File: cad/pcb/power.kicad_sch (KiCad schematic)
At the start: 12 parts

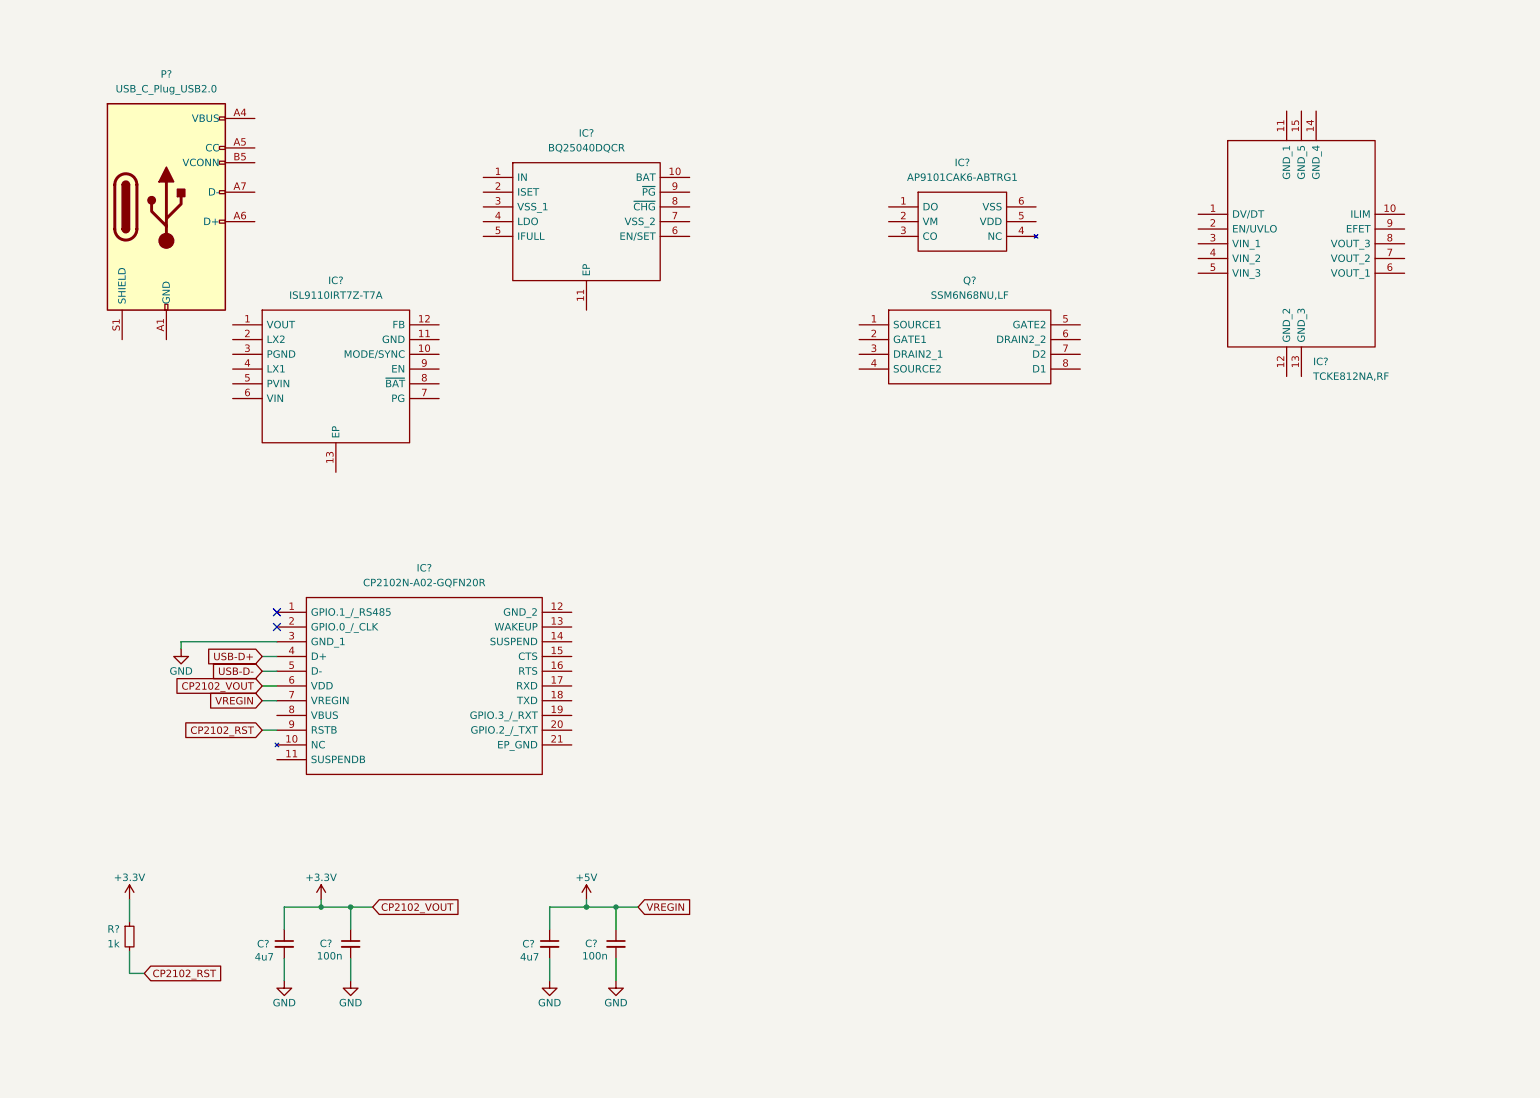
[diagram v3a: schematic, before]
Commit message: add charging & preotection circuit
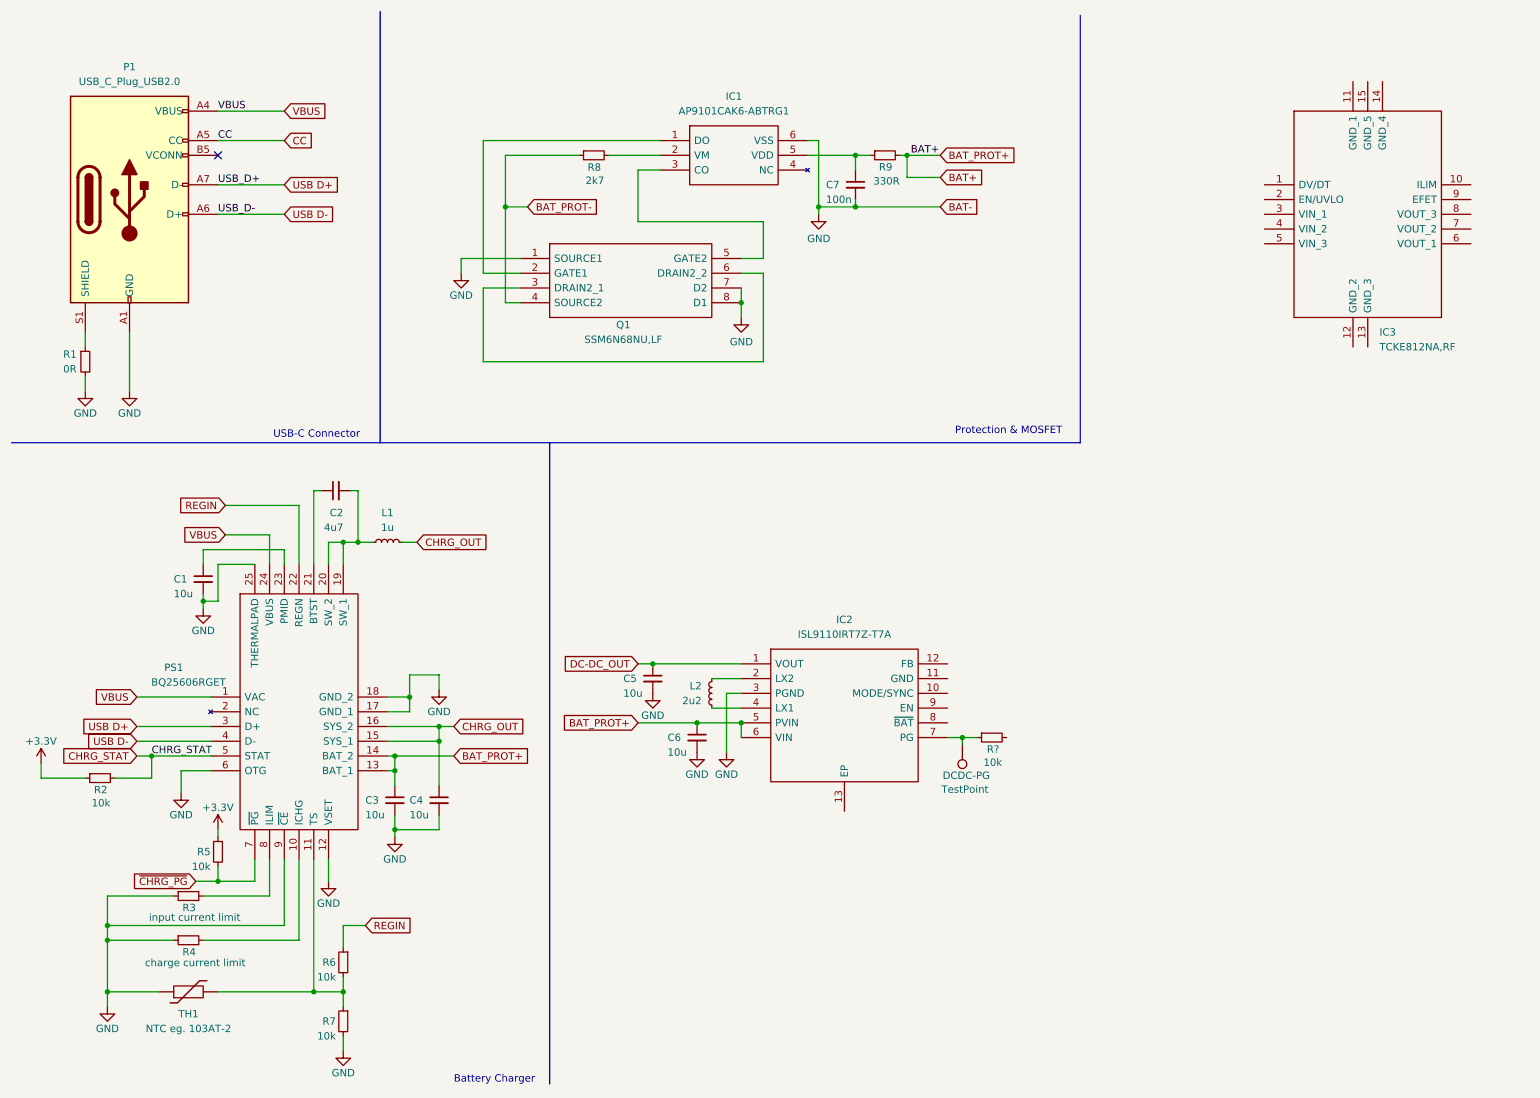
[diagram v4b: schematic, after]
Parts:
- removed C? (x2): 4u7, symbol Device:C_Small
- removed C? (x2): 100n, symbol Device:C_Small
- removed IC?: BQ25040DQCR, SON50P200X300X80-11N, symbol Battery Charger:BQ25040DQCR
- removed IC?: CP2102N-A02-GQFN20R, CP2102NA02GQFN20, symbol USB-UART Bridge:CP2102N-A02-GQFN20R
- removed R?: 1k, symbol Device:R_Small
- added C1, C3, C4, C5, C6: 10u, symbol Device:C_Small
- added C2: 4u7, symbol Device:C_Small
- added C7: 100n, symbol Device:C_Small
- added DCDC-PG: TestPoint, TestPoint:TestPoint_Pad_D2.5mm, symbol Connector:TestPoint
- added L1: 1u, symbol Device:L_Small
- added L2: 2u2, symbol Device:L_Small
- added PS1: BQ25606RGET, QFN50P400X400X100-25N, symbol Battery Charger:BQ25606RGET
- added R1: 0R, symbol Device:R_Small
- added R2, R5, R6, R7, R?: 10k, symbol Device:R_Small
- added R3: input current limit, symbol Device:R_Small
- added R4: charge current limit, symbol Device:R_Small
- added R8: 2k7, symbol Device:R_Small
- added R9: 330R, symbol Device:R_Small
- added TH1: NTC eg. 103AT-2, symbol Device:Thermistor
- gave numbers to parts that had none: 5
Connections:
- net +3.3V: now also R2.1, R5.1
- net GND: now also IC1.6 (VSS), IC2.3 (PGND), P1.A1 (GND), P1.A12 (GND), P1.B1 (GND), P1.B12 (GND), Q1.1 (SOURCE1), Q1.7 (D2), Q1.8 (D1), C1.2, C3.2, C4.2, C5.2, C6.2, C7.2, PS1.12 (VSET), PS1.17 (GND_1), PS1.18 (GND_2), PS1.25 (THERMALPAD), PS1.6 (OTG), PS1.9 (~{CE}), R1.2, R3.1, R4.1, R7.2, TH1.1
- net DC-DC_OUT: now reaches IC2.1 (VOUT)
- net DC-DC_OUT: now also C5.1
- net at IC2.2 (LX2): now also L2.1
- net at IC2.4 (LX1): now also L2.2
- net BAT+: now reaches IC2.5 (PVIN)
- net BAT+: now also IC2.6 (VIN), C3.1, C6.1, PS1.13 (BAT_1), PS1.14 (BAT_2), R9.2
- net at IC2.7 (PG): now also DCDC-PG.1, R?.1
- net VBUS: now reaches P1.A4 (VBUS), P1.A9 (VBUS), P1.B4 (VBUS), P1.B9 (VBUS)
- net VBUS: now also PS1.1 (VAC), PS1.24 (VBUS)
- net CC: now reaches P1.A5 (CC)
- net USB D-: now reaches P1.A6 (D+)
- net USB D-: now also PS1.4 (D-)
- net USB D+: now reaches P1.A7 (D-)
- net USB D+: now also PS1.3 (D+)
- net at P1.S1 (SHIELD): now also R1.1
- net at Q1.2 (GATE1): now also IC1.1 (DO)
- net at Q1.3 (DRAIN2_1): now also Q1.6 (DRAIN2_2)
- net BAT_PROT-: now reaches Q1.4 (SOURCE2)
- net BAT_PROT-: now also R8.1
- net at Q1.5 (GATE2): now also IC1.3 (CO)
- net at IC1.2 (VM): now also R8.2
- net at IC1.5 (VDD): now also C7.1, R9.1
- new net: PS1.11 (TS), R6.2, R7.1, TH1.2
- new net: C1.1, PS1.23 (PMID)
- new net: C2.1, PS1.21 (BTST)
- new net: C2.2, L1.1, PS1.19 (SW_1), PS1.20 (SW_2)
- new net: PS1.10 (ICHG), R4.2
- new net: PS1.8 (ILIM), R3.2
- new net CHRG_OUT: C4.1, L1.2, PS1.15 (SYS_1), PS1.16 (SYS_2)
- new net CHRG_STAT: PS1.5 (STAT), R2.2
- new net REGIN: PS1.22 (REGN), R6.1
- new net ~{CHRG_PG}: PS1.7 (~{PG}), R5.2
- no-connect marks 2 -> 1
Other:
- note added: "Battery Charger"
- note added: "Protection & MOSFET"
- note added: "USB-C Connector"
- moved on the sheet: IC1, IC2, IC3, P1, Q1

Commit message: add dc-dc converter, add sensors
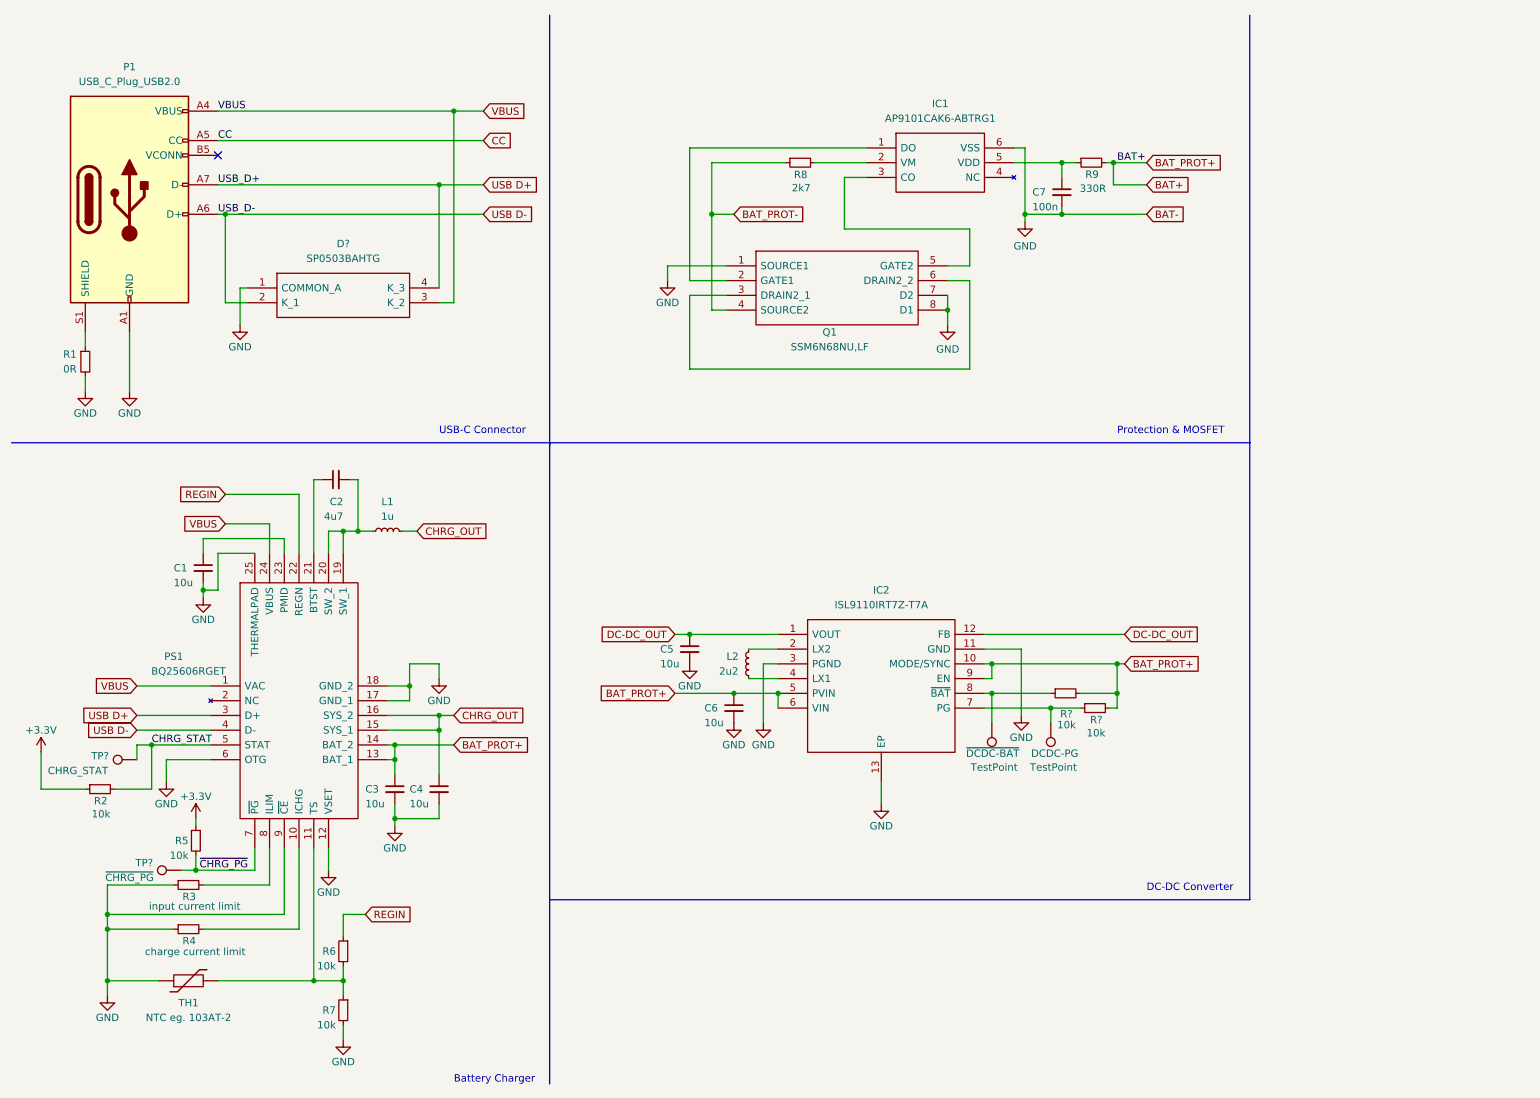
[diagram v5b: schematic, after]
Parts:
- removed IC3: TCKE812NA,RF, TCKE812NARF, symbol eFuse:TCKE812NA,RF
- added D?: SP0503BAHTG, SP0503BAHTG, symbol ESD Protection:SP0503BAHTG
- added R?: 10k, symbol Device:R_Small
- added TP?: CHRG_STAT, symbol Connector:TestPoint
- added TP?: ~{CHRG_PG}, symbol Connector:TestPoint
- added ~{DCDC-BAT}: TestPoint, TestPoint:TestPoint_Pad_D2.5mm, symbol Connector:TestPoint
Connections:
- net BAT+: now also IC2.10 (MODE/SYNC), IC2.9 (EN), R?.2, R?.2
- net CHRG_STAT: now also TP?.1
- net DC-DC_OUT: now also IC2.12 (FB)
- net GND: now also IC2.11 (GND), IC2.13 (EP), D?.1 (COMMON_A)
- net USB D+: now also D?.4 (K_3)
- net USB D-: now also D?.2 (K_1)
- net VBUS: now also D?.3 (K_2)
- net ~{CHRG_PG}: now also TP?.1
- net at IC2.8 (~{BAT}): now also R?.1, ~{DCDC-BAT}.1
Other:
- note added: "DC-DC Converter"
- moved on the sheet: C1, C2, C3, C4, C5, C6, C7, DCDC-PG, IC1, IC2, L1, L2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

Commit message: add LEDs for LED ring
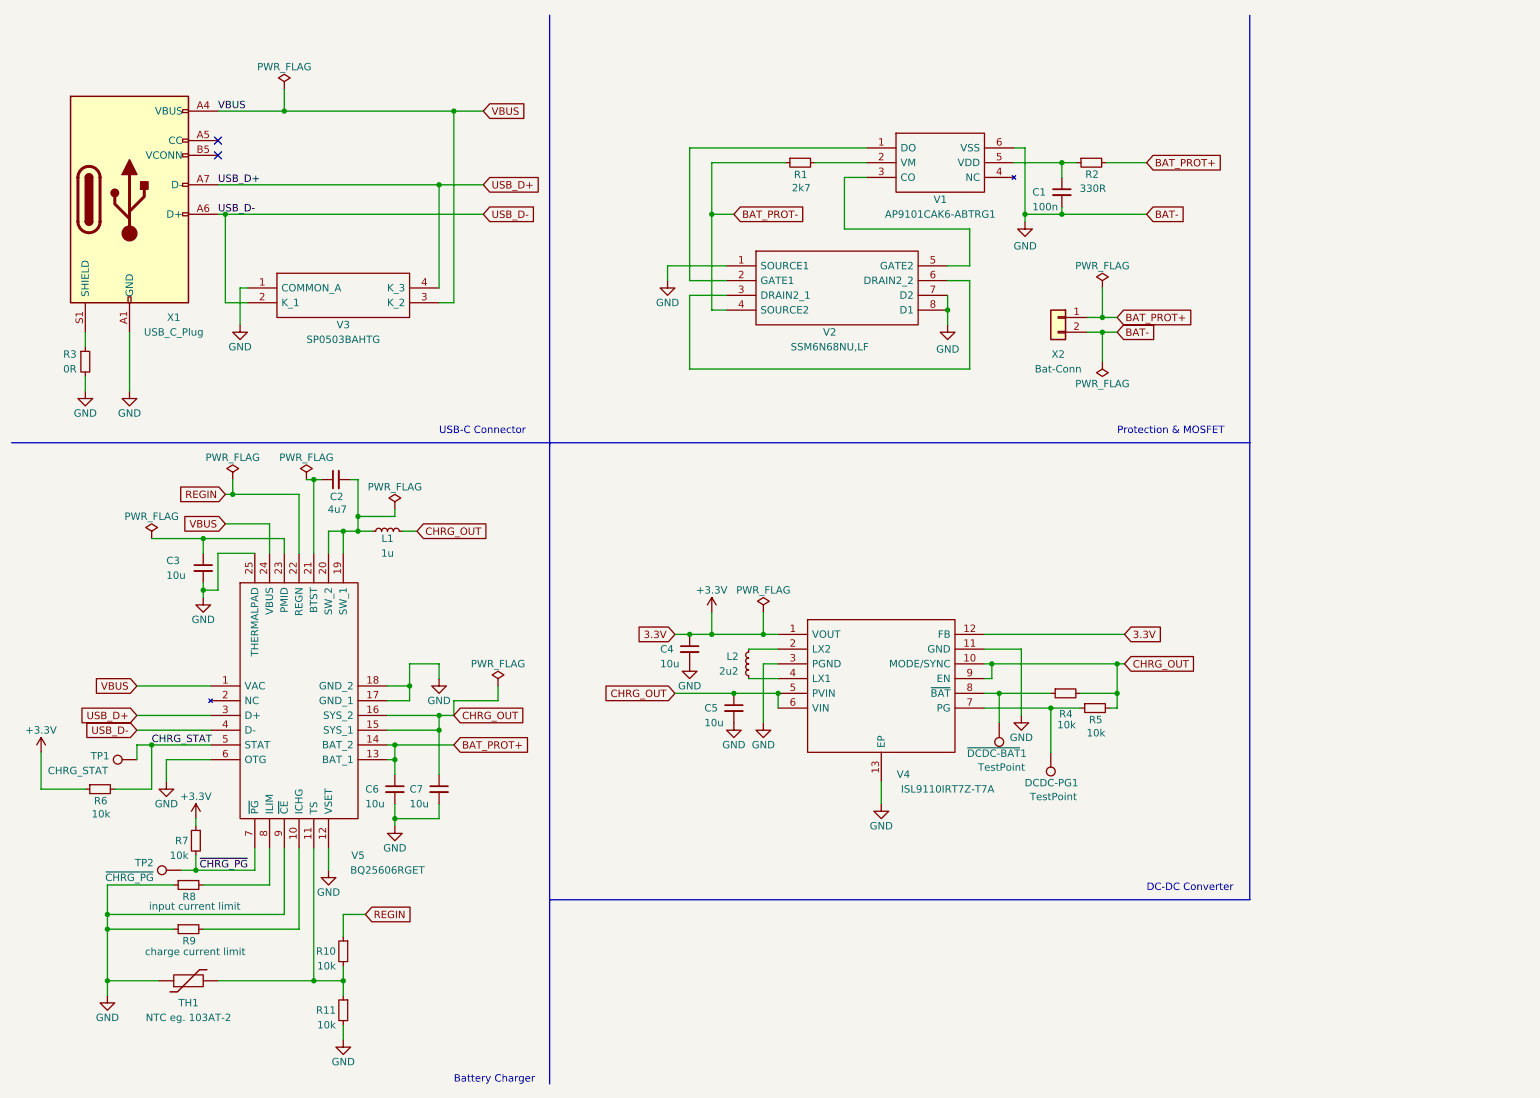
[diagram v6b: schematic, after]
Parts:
- added X2: Bat-Conn, symbol Connector_Generic:Conn_01x02
- V1: renamed from IC1; footprint SOT95P285X140-6N -> Protection:SOT95P285X140-6N
- V2: renamed from Q1; footprint SSM6N68NULF -> Mosfet:SSM6N68NULF
- V3: renamed from D?; footprint SP0503BAHTG -> ESD:SP0503BAHTG
- V4: renamed from IC2; footprint SON40P300X300X75-13N -> DC-DC:SON40P300X300X75-13N
- V5: renamed from PS1; footprint QFN50P400X400X100-25N -> Charger:QFN50P400X400X100-25N
- X1: renamed from P1; value USB_C_Plug_USB2.0 -> USB_C_Plug
- gave numbers to parts that had none: 4
- renumbered C7 to C1, C1 to C3, C5 to C4, C6 to C5, C3 to C6, C4 to C7, DCDC-PG to DCDC-PG1, R8 to R1, R6 to R10, R7 to R11, R9 to R2, R1 to R3, R2 to R6, R5 to R7, R3 to R8, R4 to R9, ~{DCDC-BAT} to ~{DCDC-BAT}1
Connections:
- net DC-DC_OUT is gone; now on net +3.3V: C4.1, V4.1 (VOUT), V4.12 (FB)
- net CHRG_OUT: now also C5.1, R4.2, R5.2, V4.10 (MODE/SYNC), V4.5 (PVIN), V4.6 (VIN), V4.9 (EN)
- net GND: now also X2.2 (Pin_2)
- removed net BAT+: C5.1, C6.1, R2.2, R4.2, R5.2, V4.10 (MODE/SYNC), V4.5 (PVIN), V4.6 (VIN), V4.9 (EN), V5.13 (BAT_1), V5.14 (BAT_2)
- net CC: no longer names the net of X1.A5 (CC)
- net USB D+ renamed USB_D+
- net USB D- renamed USB_D-
- new net BAT_PROT+: C6.1, R2.2, V5.13 (BAT_1), V5.14 (BAT_2), X2.1 (Pin_1)
- no-connect marks 1 -> 2
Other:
- moved on the sheet: DCDC-PG1, ~{DCDC-BAT}1
